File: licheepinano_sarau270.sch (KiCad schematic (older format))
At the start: 2 parts

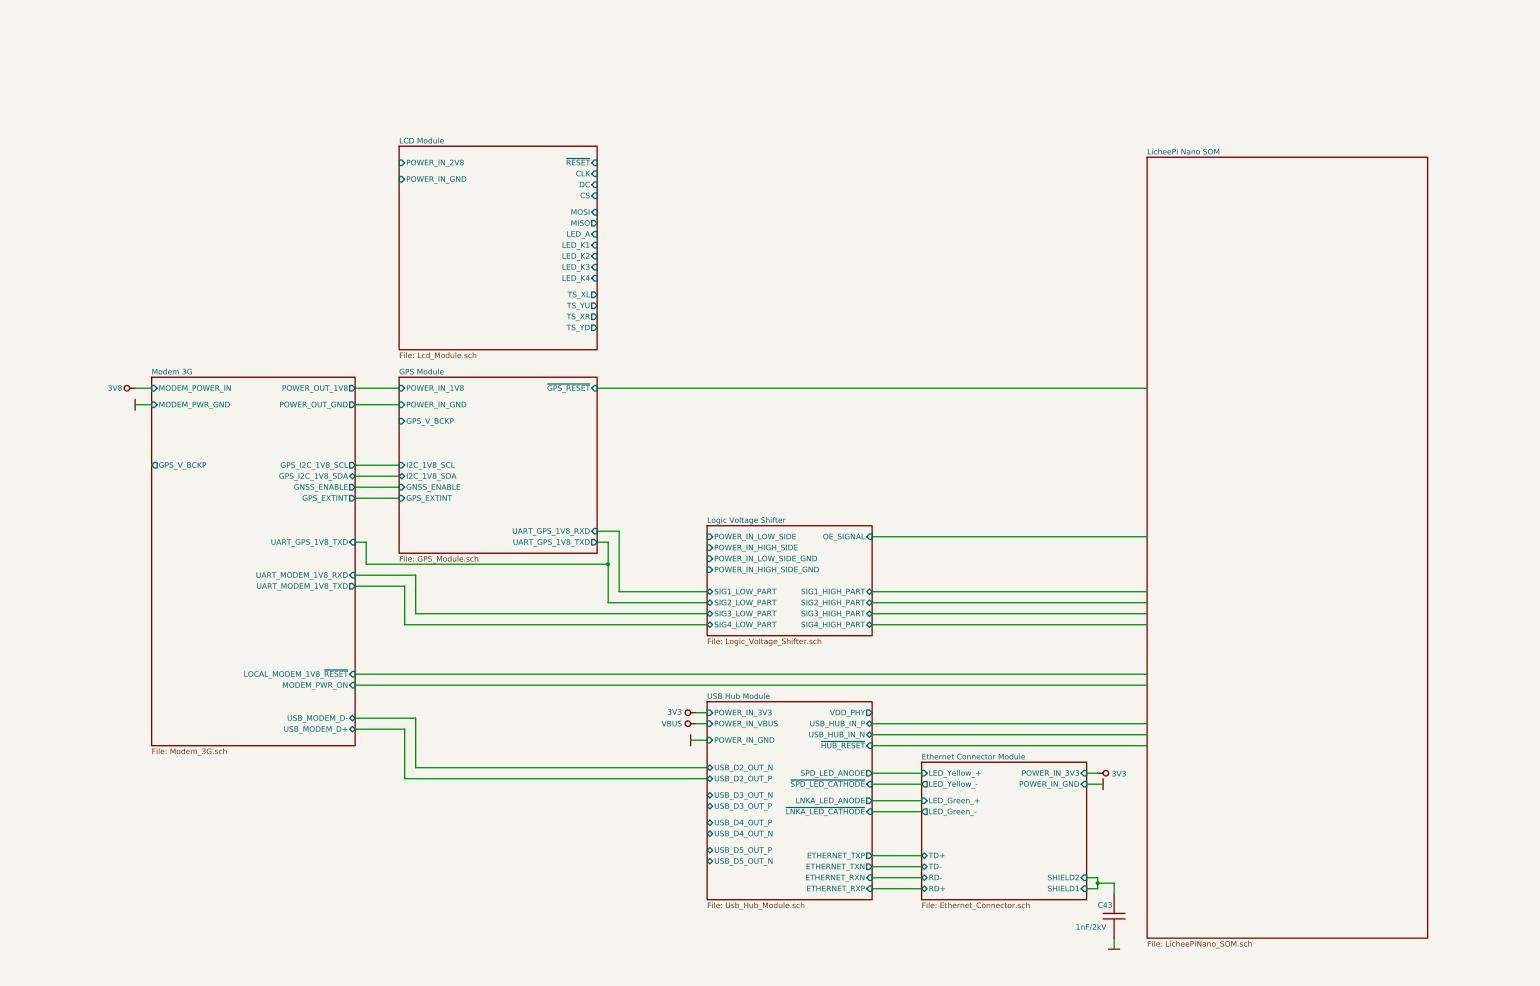
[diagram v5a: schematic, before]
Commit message: Added WiFi and figurated some components on pcb
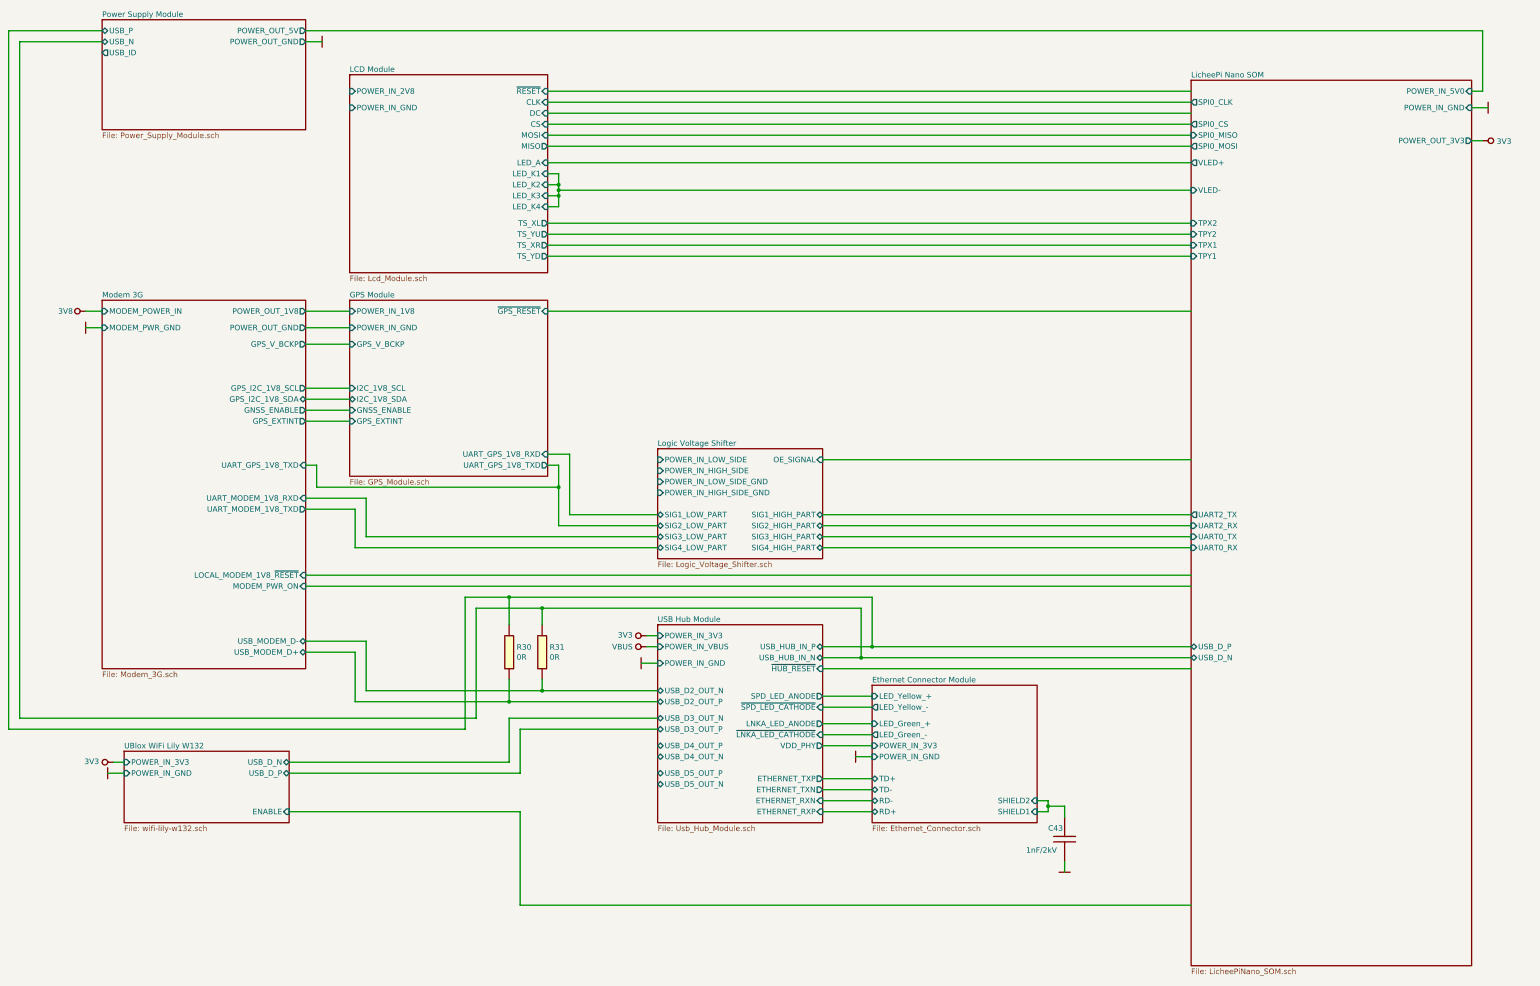
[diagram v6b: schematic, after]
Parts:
- removed Pwr?: 3V8, symbol power:3V8
- added R30, R31: 0R, Resistor_Smd_0402:0R_0402, symbol Resistors_Smd0402:0R_0402
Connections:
- net labels added: 3V8
- wire segments 61 -> 121
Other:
- moved on the sheet: C43

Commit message: Schematic finished, with check ERC
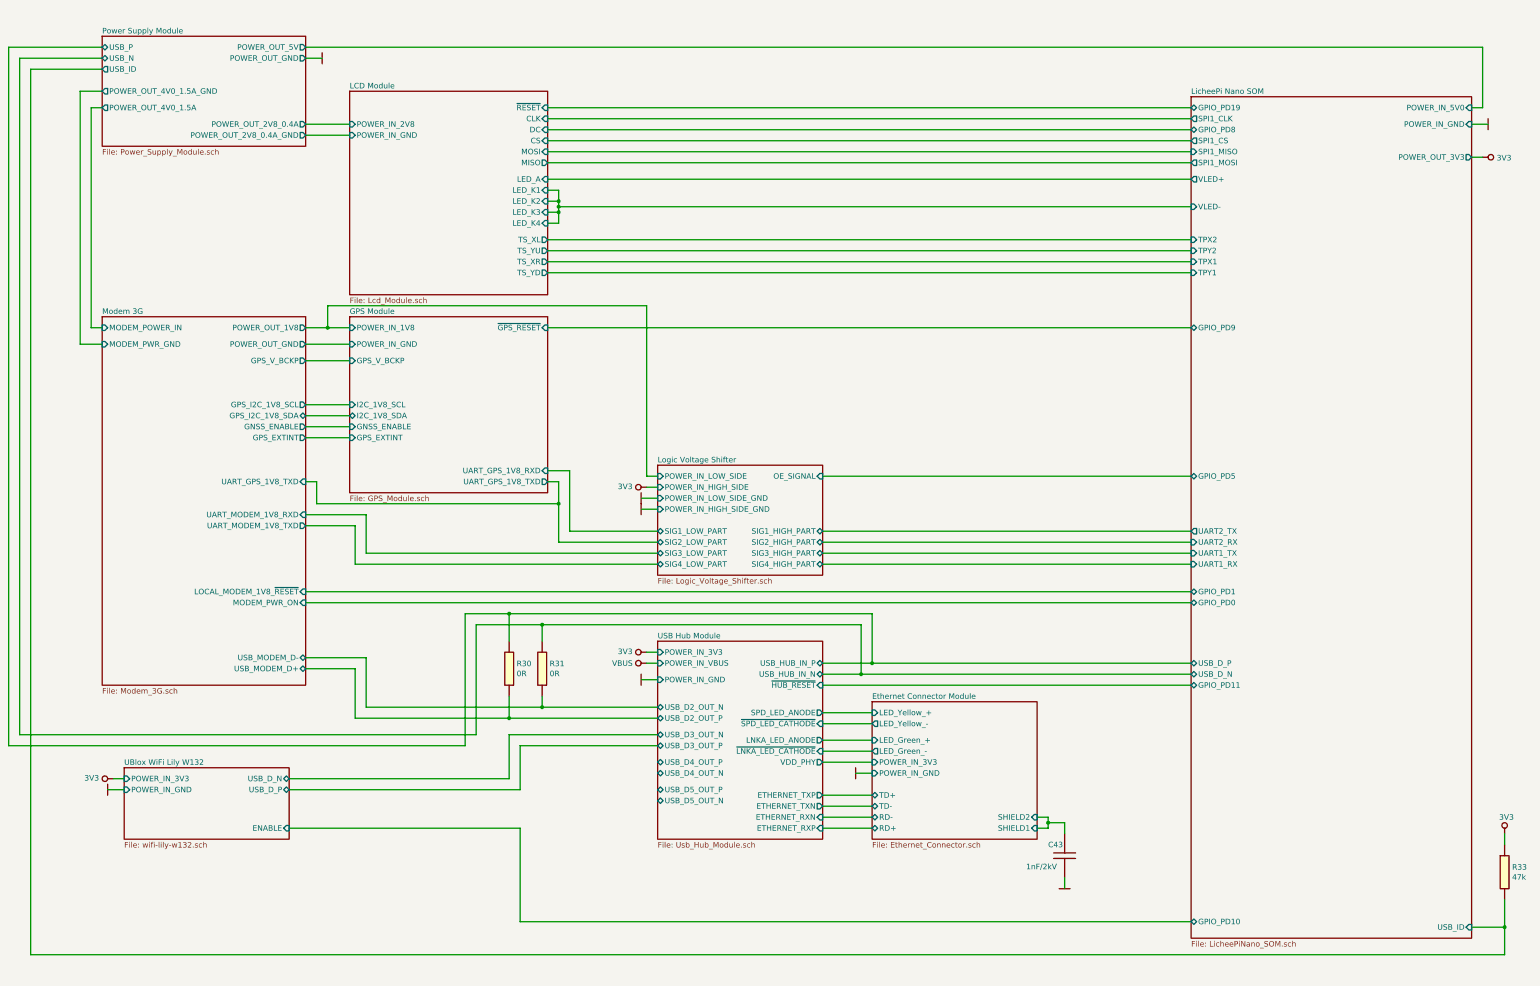
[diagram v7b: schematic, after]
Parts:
- added R33: 47k, Resistor_Smd_0402:47k_0402, symbol Resistors_Smd0402:47k_0402
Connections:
- net labels removed: 3V8
- wire segments 121 -> 142
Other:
- moved on the sheet: C43, R30, R31

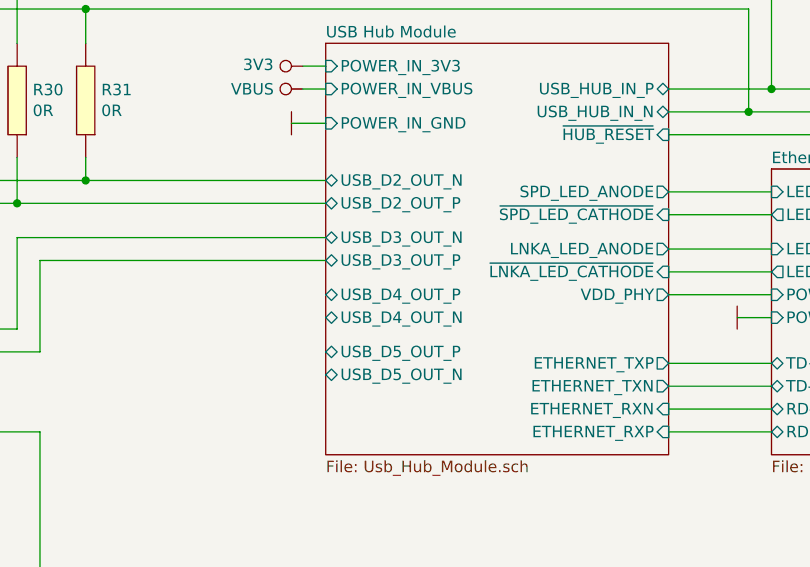
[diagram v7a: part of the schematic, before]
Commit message: Added all connections, usb and ethernet track not aligned yet, component references not aligned, gerbers not generated
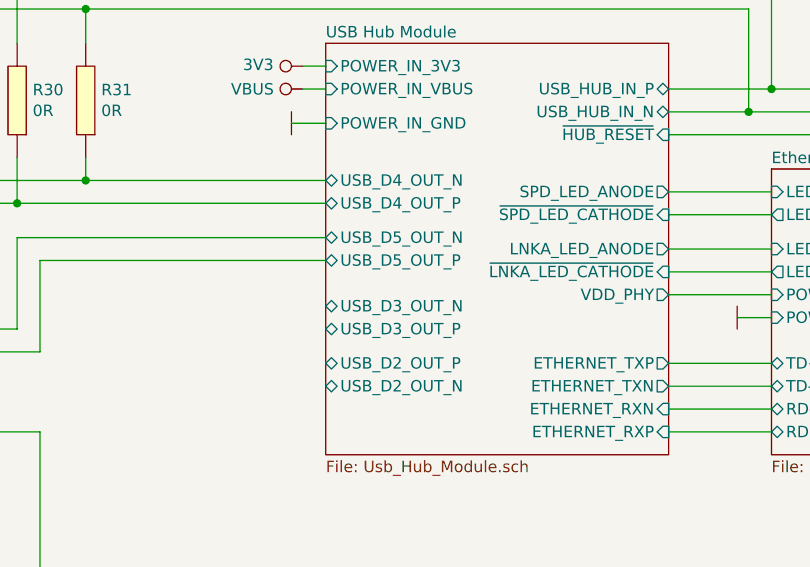
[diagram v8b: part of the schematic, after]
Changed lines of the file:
@@
 F2 "USB_HUB_IN_P" B R 9100 6850 50
 F3 "USB_HUB_IN_N" B R 9100 6950 50
-F4 "USB_D5_OUT_N" B L 7600 8100 50
-F5 "USB_D5_OUT_P" B L 7600 8000 50
-F6 "USB_D3_OUT_P" B L 7600 7600 50
-F7 "USB_D3_OUT_N" B L 7600 7500 50
-F8 "USB_D4_OUT_P" B L 7600 7750 50
-F9 "USB_D4_OUT_N" B L 7600 7850 50
-F10 "USB_D2_OUT_P" B L 7600 7350 50
-F11 "USB_D2_OUT_N" B L 7600 7250 50
+F4 "USB_D5_OUT_N" B L 7600 7500 50
+F5 "USB_D5_OUT_P" B L 7600 7600 50
+F6 "USB_D3_OUT_P" B L 7600 7900 50
+F7 "USB_D3_OUT_N" B L 7600 7800 50
+F8 "USB_D4_OUT_P" B L 7600 7350 50
+F9 "USB_D4_OUT_N" B L 7600 7250 50
+F10 "USB_D2_OUT_P" B L 7600 8050 50
+F11 "USB_D2_OUT_N" B L 7600 8150 50
 F12 "~HUB_RESET" I R 9100 7050 50
 F13 "ETHERNET_TXP" O R 9100 8050 50
